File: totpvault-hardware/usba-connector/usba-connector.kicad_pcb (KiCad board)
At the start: 2 copper layers, 19 x 42.5 mm, 27 parts, among them J3 Conn_01x06_Socket, U1 ESP32-C3, U2 HT75xx-1-SOT89, U3 CH343P, U4 USBLC6-2SC6, Y1 Crystal_GND24

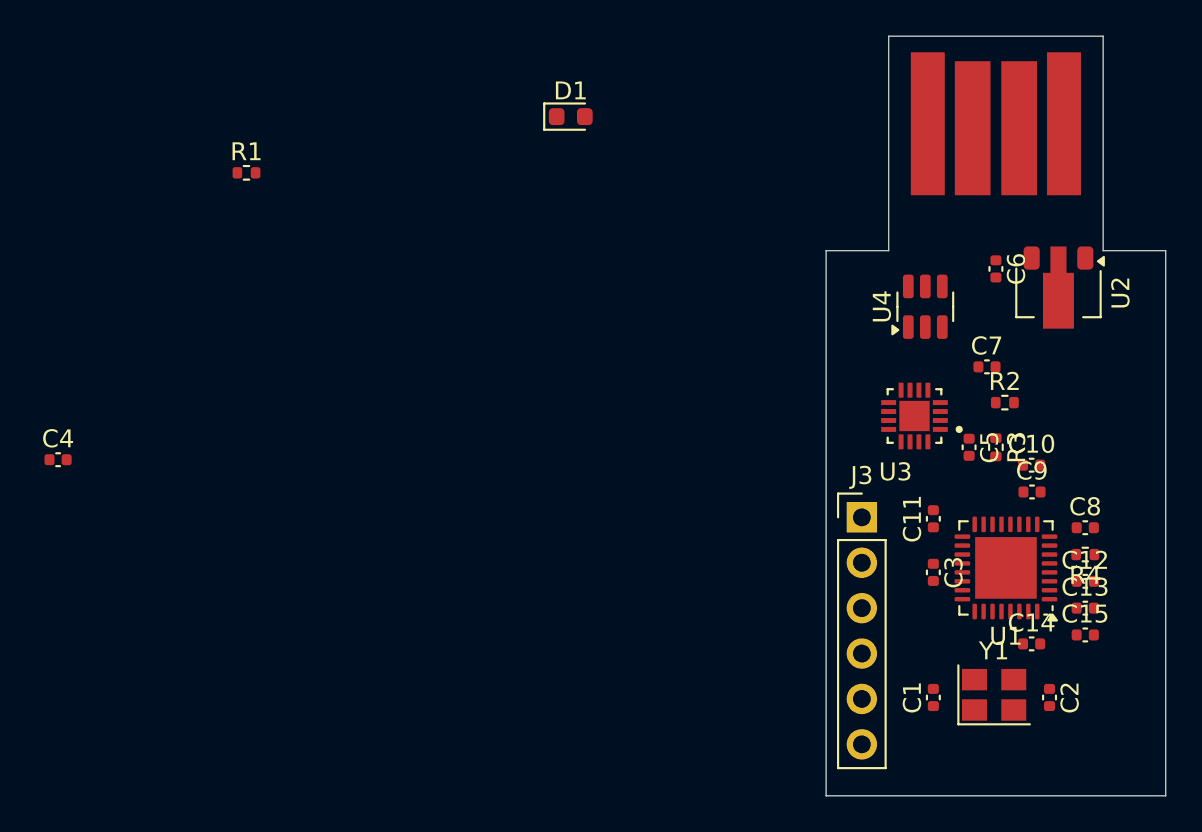
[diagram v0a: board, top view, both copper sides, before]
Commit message: Finalized USB-A PCB
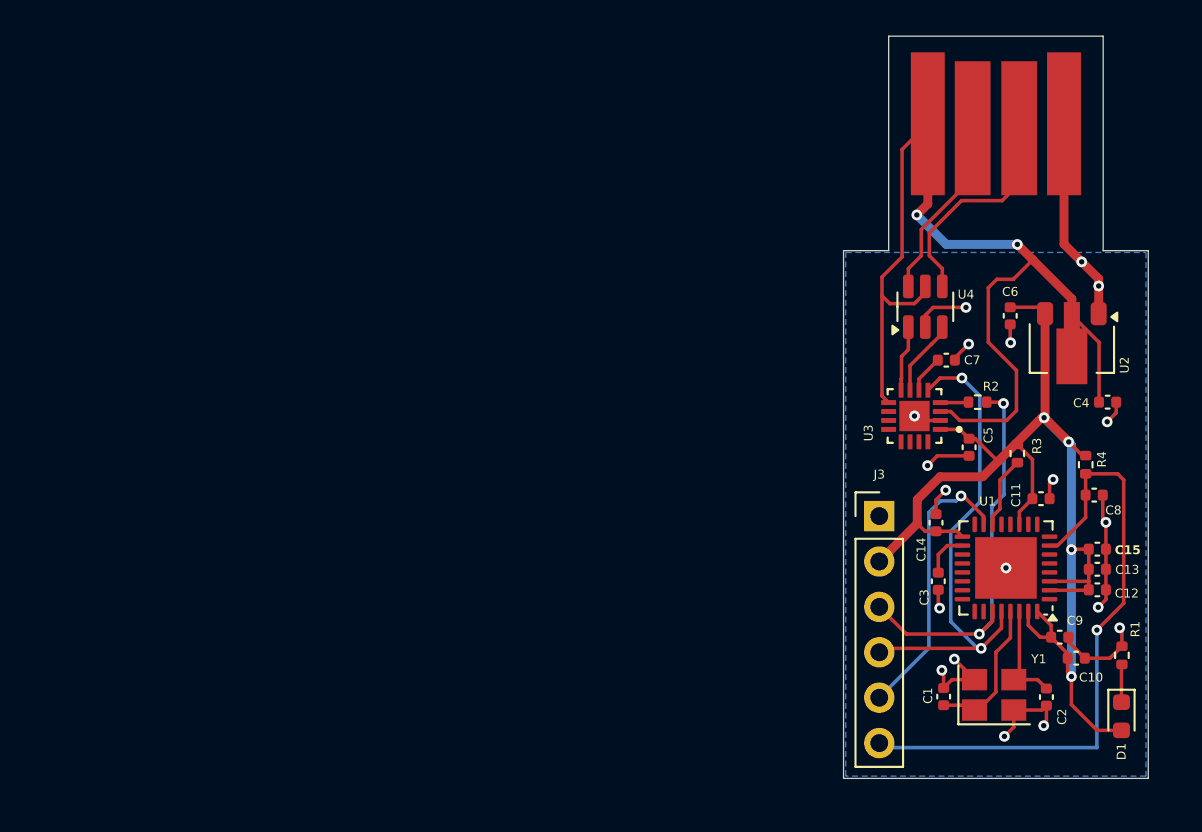
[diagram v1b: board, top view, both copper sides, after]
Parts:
- U3: footprint Custom:CH343P -> Misc:CH343P
- moved C4 58.8 mm to (111.8, 50.5)
- moved R1 55.9 mm to (112.5, 64.6), turned to -90 degrees
- moved D1 45.6 mm to (112.5, 68.0), turned to -90 degrees
- moved C10 11.1 mm to (110.0, 64.8)
- moved C14 8.64 mm to (102.2, 57.2), turned to 90 degrees
- moved C9 8.27 mm to (109.1, 63.6)
- moved C11 6.13 mm to (108.0, 55.9), turned to 0 degrees
- moved R4 5.03 mm to (110.5, 54.0), turned to -90 degrees
- moved C15 4.85 mm to (111.2, 58.7)
- moved U2 3.20 mm to (109.8, 47.5)
- moved C6 2.74 mm to (106.3, 45.6)
- moved C7 2.31 mm to (102.7, 48.1)
- moved C13 2.28 mm to (111.2, 59.8)
- moved C8 1.89 mm to (111.0, 55.7)
- moved R2 1.53 mm to (104.5, 50.5)
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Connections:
- J3 pad 1: BOOT -> GND
- J3 pad 2: RESET -> VDD3P3
- J3 pad 3: TXD -> TXD_uC
- J3 pad 5: VDD3P3 -> BOOT
- J3 pad 6: GND -> RESET
- R2 pad 2: Net-(U1-U0RXD/GPIO20) -> TXD_uC
- U1 pad 27: Net-(U1-U0RXD/GPIO20) -> TXD_uC
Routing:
- net VDD3P3: track 0.00 -> 70.8 mm, vias 0 -> 4
- net VBUS: track 0.00 -> 57.8 mm, vias 0 -> 2
- net GND: track 0.00 -> 46.9 mm, vias 0 -> 19
- net RESET: track 0.00 -> 35.3 mm, vias 0 -> 1
- net RXD: track 0.00 -> 27.5 mm, vias 0 -> 2
- net TXD_uC: track 0.00 -> 22.2 mm, vias 0 -> 2
- net BOOT: track 0.00 -> 15.9 mm, vias 0 -> 1
- net /D+: track 0.00 -> 12.6 mm
- net /D-: track 0.00 -> 10.3 mm
- net Net-(U1-XTAL_N): track 0.00 -> 8.30 mm
- net Net-(U1-XTAL_P): track 0.00 -> 5.97 mm
- net /EMI_D+: track 0.00 -> 4.28 mm
- net Net-(U1-GPIO8): track 0.00 -> 4.03 mm
- net /EMI_D-: track 0.00 -> 3.70 mm
- net Net-(U1-VDD_SPI/GPIO11): track 0.00 -> 2.57 mm
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- added copper zone on B.Cu, net GND
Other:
- board size 19 x 42.5 mm -> 17.1 x 41.5 mm

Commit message: Order ready for USB-A
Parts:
- added TP1: TestPoint_Probe, TestPoint:TestPoint_Pad_D1.0mm, B.Cu at (105.5, 44.0)
- added TP2: TestPoint_Probe, TestPoint:TestPoint_Pad_D1.0mm, B.Cu at (108.5, 44.0)
- added TP3: TestPoint_Probe, TestPoint:TestPoint_Pad_D1.0mm, B.Cu at (109.5, 50.0)
- C4, C6: value 22uF -> 10uF
- U3: footprint Misc:CH343P -> Custom:CH343P
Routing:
- net VBUS: track 57.8 -> 60.6 mm
- net VDD3P3: track 70.8 -> 72.7 mm
- net /D-: track 10.3 -> 11.4 mm
- net /EMI_D-: track 3.70 -> 4.23 mm

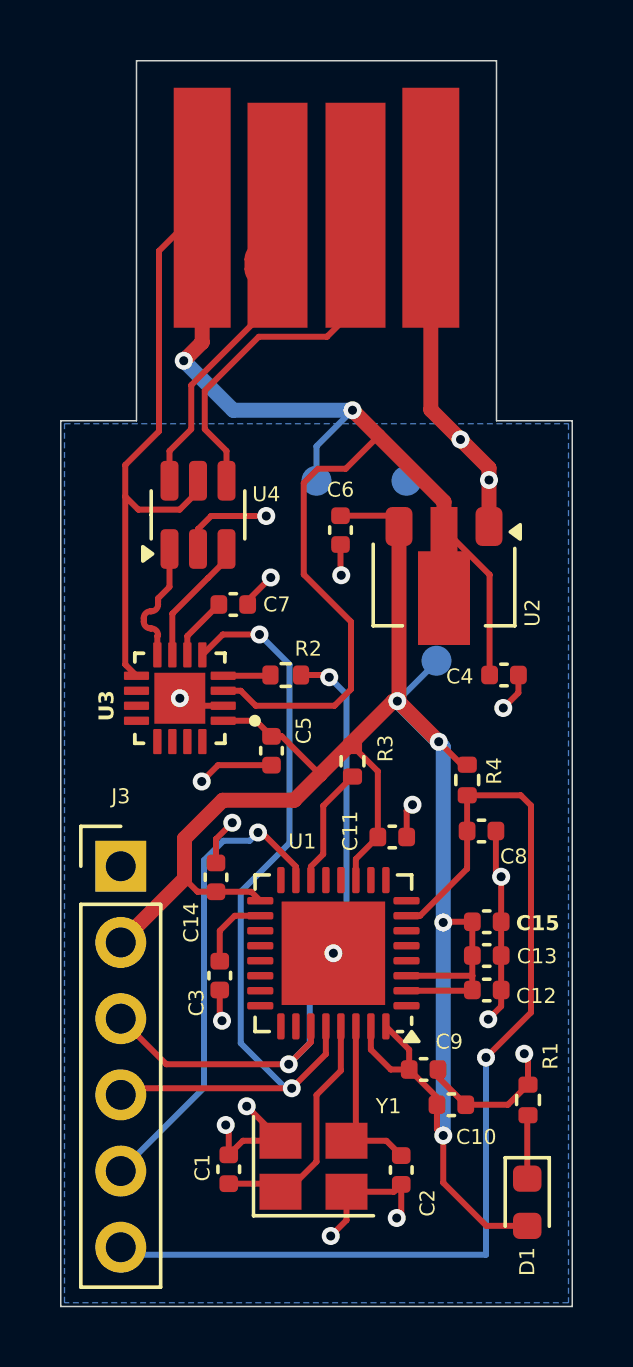
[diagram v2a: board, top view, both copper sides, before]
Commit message: Modified USB-A connector to use a physical connector instead of PCB slice due to pricing of ordering 2mm gold-plated PCBs
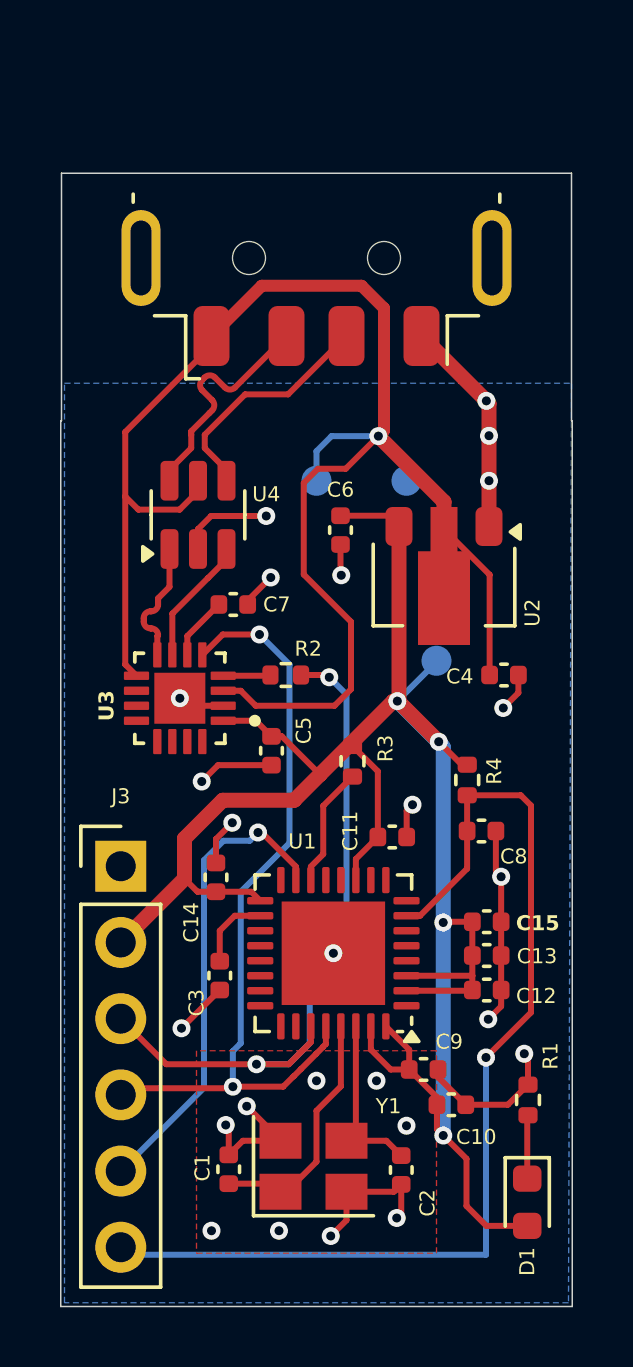
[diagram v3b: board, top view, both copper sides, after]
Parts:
- X1: footprint Custom:usb-PCB -> Connector_USB:USB_A_Molex_48037-2200_Horizontal
- moved X1 1.80 mm to (105.5, 28.2), turned to 90 degrees
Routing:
- net VBUS: track 60.6 -> 55.1 mm, vias 2 -> 1
- net /D+: track 12.6 -> 7.92 mm
- net /D-: track 11.4 -> 7.89 mm
- net GND: track 46.9 -> 43.5 mm, vias 19 -> 25
- net TXD_uC: track 22.7 -> 23.8 mm
- net RXD: track 27.5 -> 26.6 mm
- added copper zone on F.Cu, net GND
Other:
- board size 17.1 x 41.5 mm -> 17.1 x 37.8 mm
